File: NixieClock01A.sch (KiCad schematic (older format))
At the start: 47 parts, among them J1 Conn_01x10, J13 Conn_02x18_Odd_Even, J14 Conn_01x08, J15 Conn_01x08, J2 Conn_01x08, J3 Conn_01x08, J4 Conn_01x08, J6 Conn_01x01_Male, J8 Conn_01x01_Male, Q1 FQD10N20CTM, SW1 SW_Push, SW2 SW_Push, SW3 SW_Push, U1 DS3231, U4 LM3478

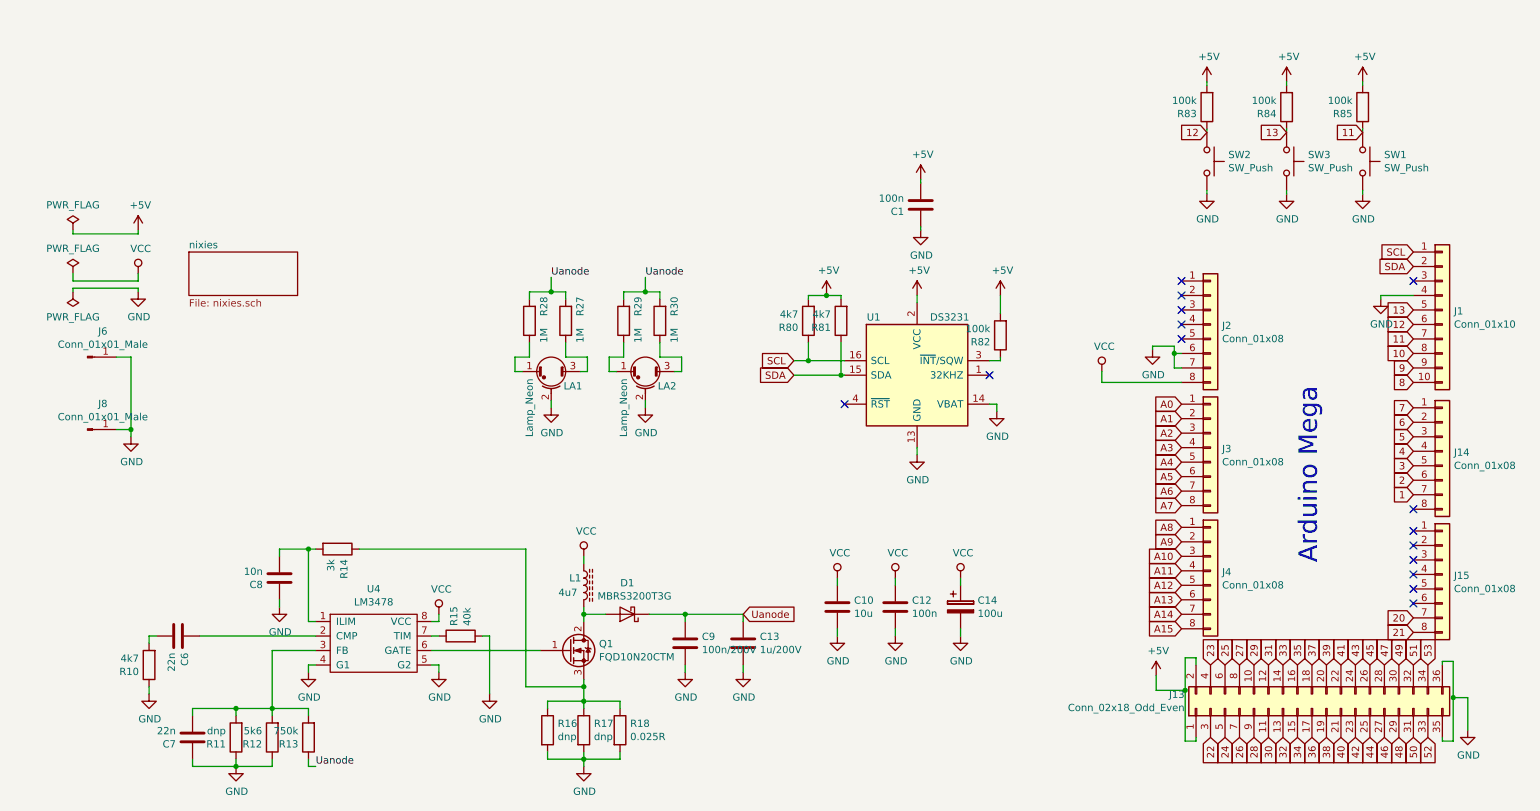
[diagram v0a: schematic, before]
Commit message: First version of working firmware. Small components values change
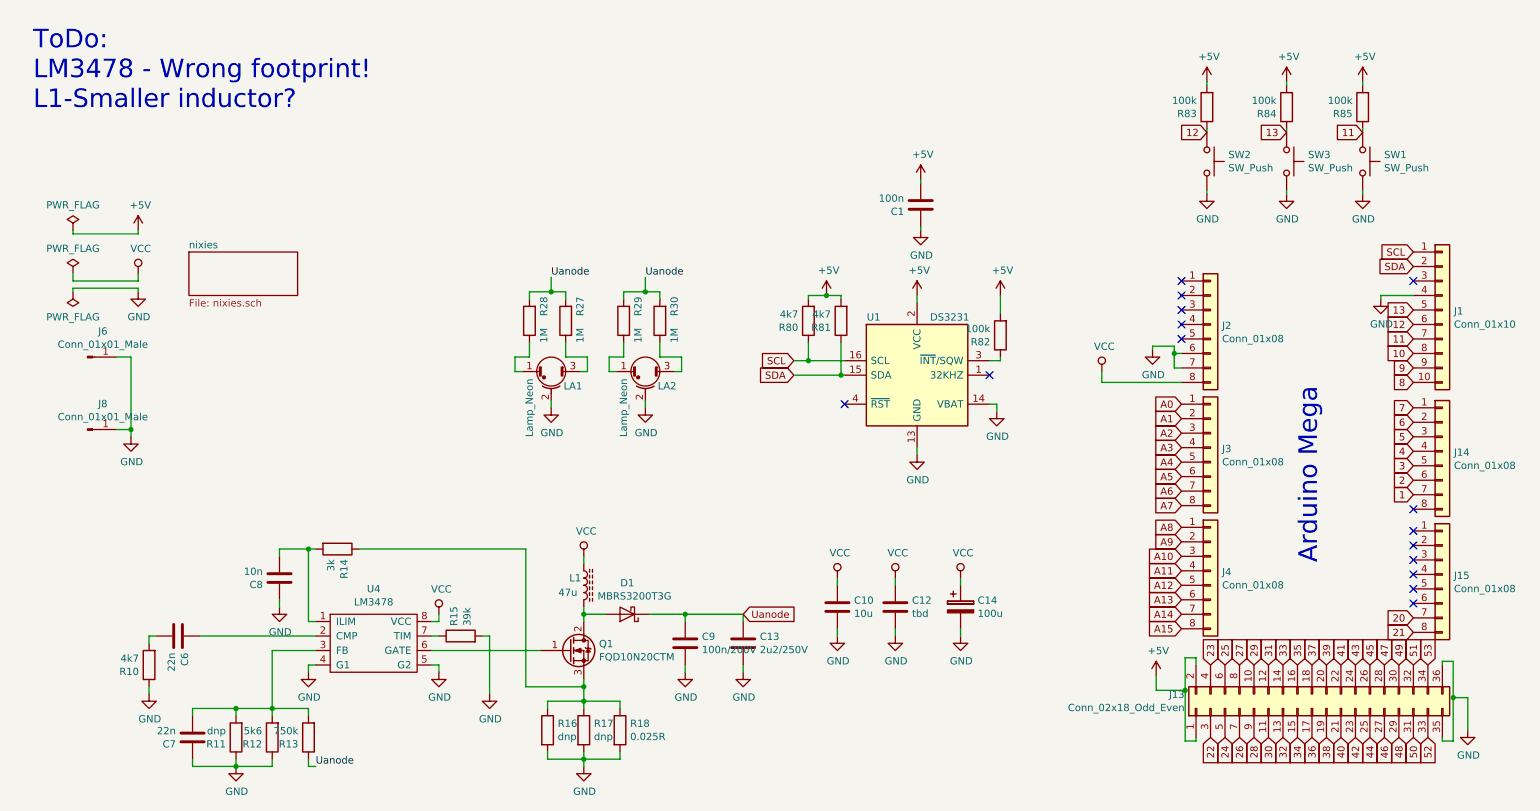
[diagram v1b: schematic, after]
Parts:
- C12: value 100n -> tbd
- C13: value 1u/200V -> 2u2/250V
- L1: value 4u7 -> 47u
- R15: value 40k -> 39k
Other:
- note added: "ToDo:\nLM3478 - Wrong footprint!\nL1-Smaller inductor?"
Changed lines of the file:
@@
 EESchema Schematic File Version 4
 LIBS:NixieClock01A-cache
-EELAYER 29 0
+EELAYER 26 0
 EELAYER END
 $Descr A4 11693 8268
@@
 P 3800 4850
 F 0 "R15" H 3870 4896 50  0000 L CNN
-F 1 "40k" H 3870 4805 50  0000 L CNN
+F 1 "39k" H 3870 4805 50  0000 L CNN
 F 2 "Resistor_SMD:R_0603_1608Metric" V 3730 4850 50  0001 C CNN
 F 3 "~" H 3800 4850 50  0001 C CNN
@@
 P 4650 4500
 F 0 "L1" H 4550 4550 50  0000 L CNN
-F 1 "4u7" H 4475 4450 50  0000 L CNN
+F 1 "47u" H 4475 4450 50  0000 L CNN
 F 2 "Inductor_SMD:L_Wuerth_WE-PD-Typ-LS_Handsoldering" H 4650 4500 50  0001 C CNN
 F 3 "~" H 4650 4500 50  0001 C CNN
@@
 P 6800 4650
 F 0 "C12" H 6915 4696 50  0000 L CNN
-F 1 "100n" H 6915 4605 50  0000 L CNN
+F 1 "tbd" H 6915 4605 50  0000 L CNN
 F 2 "Capacitor_SMD:C_0603_1608Metric" H 6838 4500 50  0001 C CNN
 F 3 "~" H 6800 4650 50  0001 C CNN
@@
 P 5750 4900
 F 0 "C13" H 5865 4946 50  0000 L CNN
-F 1 "1u/200V" H 5865 4855 50  0000 L CNN
+F 1 "2u2/250V" H 5865 4855 50  0000 L CNN
 F 2 "Capacitor_SMD:C_2220_5650Metric" H 5788 4750 50  0001 C CNN
 F 3 "~" H 5750 4900 50  0001 C CNN
@@
 Text GLabel 10025 1375 0    50   Input ~ 0
 11
+Text Notes 850  1225 0    128  ~ 0
+ToDo:\nLM3478 - Wrong footprint!\nL1-Smaller inductor?
 $EndSCHEMATC

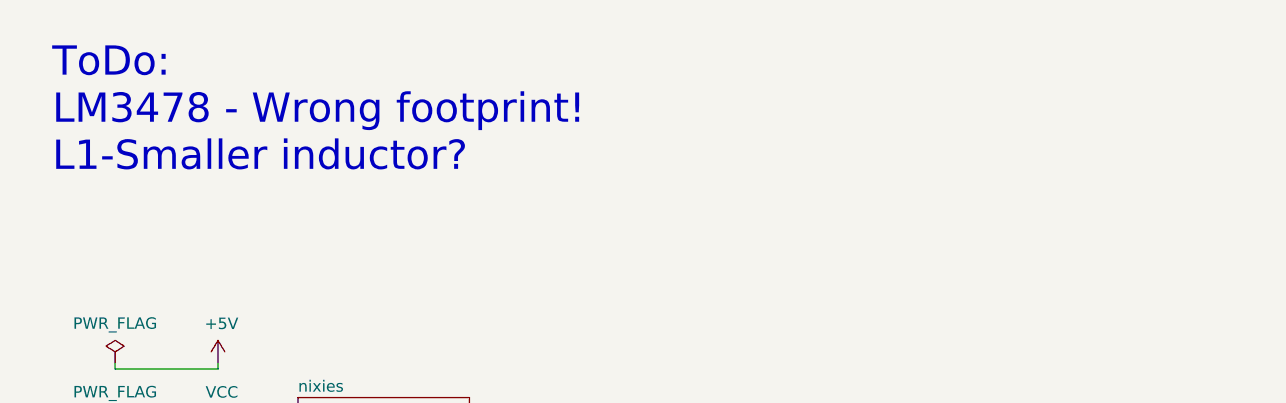
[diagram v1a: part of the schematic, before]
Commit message: Changed BJT base resistor values, Added photo, Added new inspiration schematic, Changed README
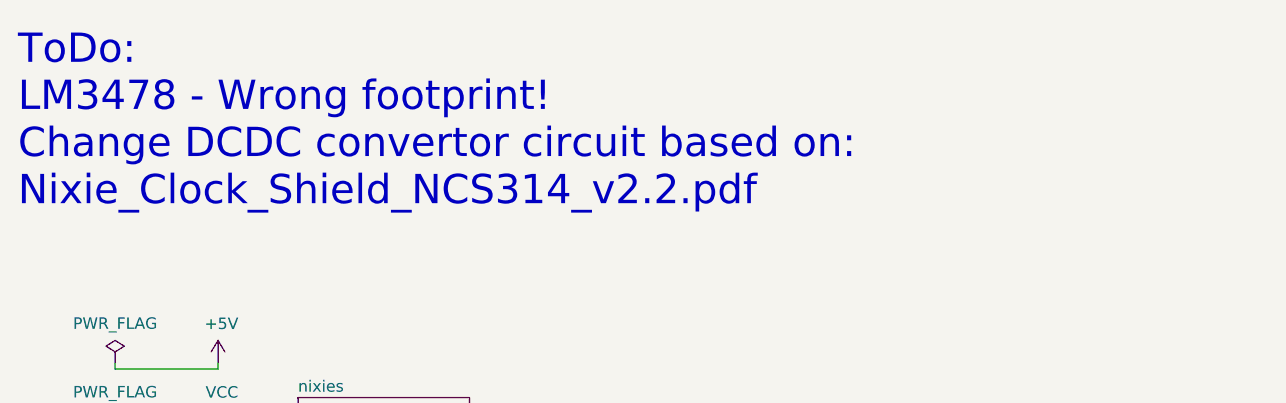
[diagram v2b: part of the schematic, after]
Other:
- note added: "ToDo:\nLM3478 - Wrong footprint!\nChange DCDC convertor circuit based on: \nNixie_Clock_Shield_NCS314_v2.2.pdf"
- note removed: "ToDo:\nLM3478 - Wrong footprint!\nL1-Smaller inductor?"
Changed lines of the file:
@@
 Text GLabel 10025 1375 0    50   Input ~ 0
 11
-Text Notes 850  1225 0    128  ~ 0
-ToDo:\nLM3478 - Wrong footprint!\nL1-Smaller inductor?
+Text Notes 700  1375 0    128  ~ 0
+ToDo:\nLM3478 - Wrong footprint!\nChange DCDC convertor circuit based on: \nNixie_Clock_Shield_NCS314_v2.2.pdf
 $EndSCHEMATC

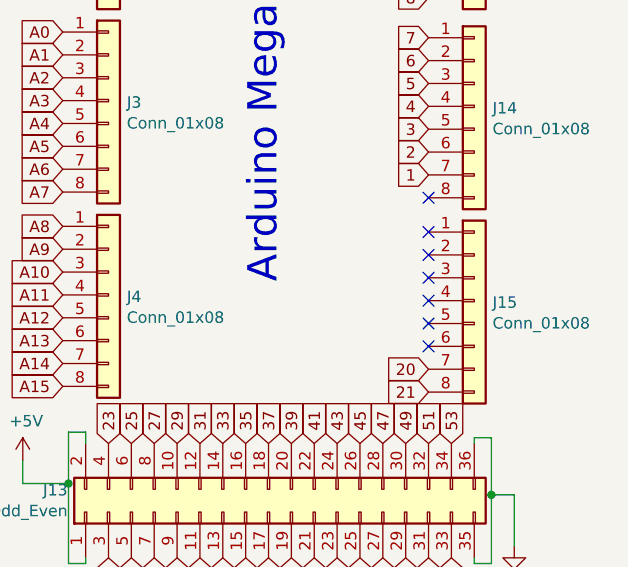
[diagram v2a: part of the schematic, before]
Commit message: Solved I2C, UART conflict
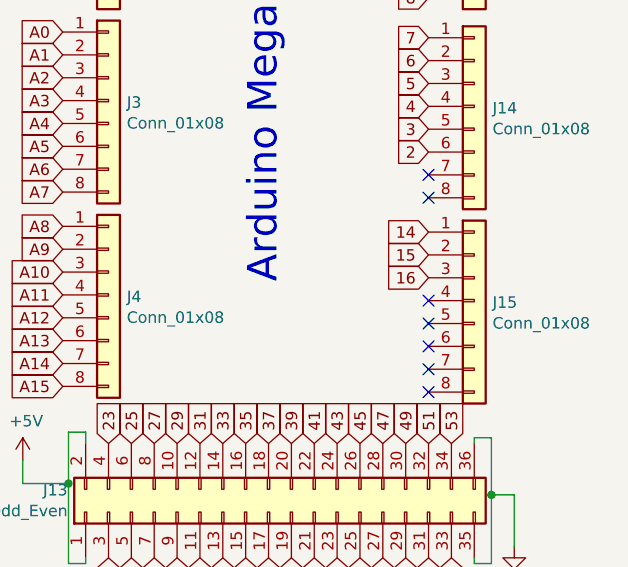
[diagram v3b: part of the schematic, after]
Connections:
- net 14: now reaches J15.1 (Pin_1)
- net 15: now reaches J15.2 (Pin_2)
- net 16: now reaches J15.3 (Pin_3)
- net 1: no longer names the net of J14.7 (Pin_7)
- net 20: no longer names the net of J15.7 (Pin_7)
- net 21: no longer names the net of J15.8 (Pin_8)
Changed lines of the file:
@@
 Text GLabel 10375 3275 0    50   Input ~ 0
 7
-Text GLabel 10375 4825 0    50   Input ~ 0
-21
-Text GLabel 10375 4725 0    50   Input ~ 0
-20
 Text GLabel 8775 4800 0    50   Input ~ 0
 A15
@@
 NoConn ~ 8775 2700
 NoConn ~ 10375 3975
-NoConn ~ 10375 4125
-NoConn ~ 10375 4225
-NoConn ~ 10375 4325
 NoConn ~ 10375 4425
 NoConn ~ 10375 4525
@@
 Text GLabel 10375 3775 0    50   Input ~ 0
 2
-Text GLabel 10375 3875 0    50   Input ~ 0
-1
 $Comp
 L NixieClock01A-rescue:SW_Push-Switch SW1
@@
 Text Notes 700  1375 0    128  ~ 0
 ToDo:\nLM3478 - Wrong footprint!\nChange DCDC convertor circuit based on: \nNixie_Clock_Shield_NCS314_v2.2.pdf
+NoConn ~ 10375 3875
+Text GLabel 10375 4125 0    50   Input ~ 0
+14
+Text GLabel 10375 4225 0    50   Input ~ 0
+15
+Text GLabel 10375 4325 0    50   Input ~ 0
+16
+NoConn ~ 10375 4725
+NoConn ~ 10375 4825
 $EndSCHEMATC
